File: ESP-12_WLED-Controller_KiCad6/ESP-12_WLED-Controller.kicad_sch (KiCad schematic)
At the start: 24 parts, among them J1 Conn_01x04_Male, J2 Conn_01x04_Male, Q1 IRLML6344, Q2 IRF7410, SW1 SW_RST, U1 TS1117-3.3, U2 ESP-12E, U4 74LVC1G125

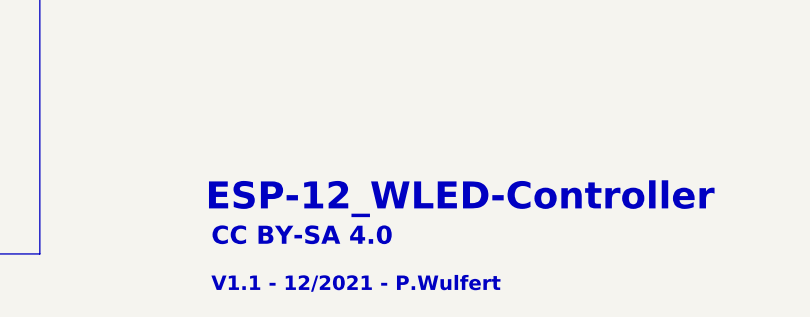
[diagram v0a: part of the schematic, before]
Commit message: V1.2
change Gate Resistor to 300 Ohm
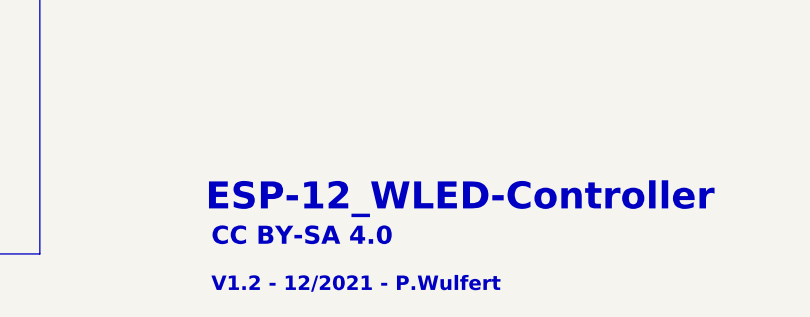
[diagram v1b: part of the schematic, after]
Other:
- note added: "V1.2 - 12/2021 - P.Wulfert"
- note removed: "V1.1 - 12/2021 - P.Wulfert"
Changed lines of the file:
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@@
     (effects (font (size 0.889 0.889)) (justify left bottom))
   )
-  (text "V1.1 - 12/2021 - P.Wulfert" (at 178.435 180.34 0)
+  (text "V1.2 - 12/2021 - P.Wulfert" (at 178.435 180.34 0)
     (effects (font (size 1.6002 1.6002) (thickness 0.32) bold) (justify left bottom))
   )

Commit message: Update to V2.0
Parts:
- removed J2: Conn_01x04_Male, Connector_PinHeader_2.54mm:PinHeader_1x04_P2.54mm_Vertical, symbol Connector:Conn_01x04_Male
- added J2: Conn_01x05_Male, Connector_PinHeader_2.54mm:PinHeader_1x05_P2.54mm_Vertical, symbol Connector:Conn_01x05_Male
- added JP2: Jumper_2_Open, Jumper:SolderJumper-2_P1.3mm_Open_TrianglePad1.0x1.5mm, symbol Jumper:Jumper_2_Open
- added aC2: 100µF, Capacitor_SMD:C_0805_2012Metric_Pad1.18x1.45mm_HandSolder, symbol Device:C
- C1, C2: LCSC (none) -> C1713
- C3: LCSC (none) -> C49678
- C4: LCSC (none) -> C189254
- D1: LCSC (none) -> C2480
- JP1: LCSC (none) -> C390678
- Q1: LCSC (none) -> C693370
- Q2: LCSC (none) -> C152423
- R1, R2, R3, R4, R5, R7, R8, R9: LCSC (none) -> C17617
- R6: LCSC (none) -> C114564
- SW1: LCSC (none) -> C329185
- U1: LCSC (none) -> C410833
- U2: LCSC (none) -> C82891
- U4: LCSC (none) -> C12518
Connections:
- net +3V3: now also J2.4 (Pin_4), aC2.1
- net GND: now also J2.1 (Pin_1), aC2.2
- net GPIO4_5: now also JP2.1 (A)
- net RX: now also J2.3 (Pin_3)
- net TX: now also J2.2 (Pin_2)
- net A0: now reaches U2.2 (ADC)
- net A0: now also J2.5 (Pin_5)
- net DATA: now reaches J1.3 (Pin_3), R6.1
- net DATA: now also JP2.2 (B)
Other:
- note added: "Additional Capacitor Value depends on taken LDO."
- note added: "Bypass jumper for R6, if any problems with data signal."
- note added: "Expose A0 Analog input can be used for sound reactive features."
- note added: "Resistor value is not fixed! In some cases it's better to decrease the value. In very rare conditions, the strip will just run without a resistor."
- note added: "THT P-MOSFET Alternative to the SOIC type."
- note added: "V2.0 - 01/2022 - P.Wulfert"
- note removed: "V1.2 - 12/2021 - P.Wulfert"
- note removed: "use here an alternative THT P-MOSFET"
- moved on the sheet: C3, R7, R9, SW1, altQ2

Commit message: Update to V1.3
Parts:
- removed J1: Conn_01x04_Male, TerminalBlock_Phoenix:TerminalBlock_Phoenix_MKDS-1,5-4-5.08_1x04_P5.08mm_Horizontal, symbol Connector:Conn_01x04_Male
- removed J2: Conn_01x05_Male, Connector_PinHeader_2.54mm:PinHeader_1x05_P2.54mm_Vertical, symbol Connector:Conn_01x05_Male
- removed altQ2: alt. MOSFET, Package_TO_SOT_THT:TO-220-3_Vertical, symbol Transistor_FET:IRF9540N
- added C5: 100nF, Capacitor_SMD:C_0805_2012Metric_Pad1.18x1.45mm_HandSolder, symbol Device:C
- added J1: Screw_Terminal_01x05, TerminalBlock:TerminalBlock_bornier-5_P5.08mm, symbol Connector:Screw_Terminal_01x05
- added J2: Conn_01x04_Male, Connector_PinSocket_2.54mm:PinSocket_1x04_P2.54mm_Vertical, symbol Connector:Conn_01x04_Male
- C1, C3: footprint Capacitor_SMD:C_0805_2012Metric_Pad1.15x1.40mm_HandSolder -> Capacitor_SMD:C_0805_2012Metric_Pad1.18x1.45mm_HandSolder
- C2: value 10µF -> 47F; footprint Capacitor_SMD:C_0805_2012Metric_Pad1.15x1.40mm_HandSolder -> Capacitor_SMD:C_0805_2012Metric_Pad1.18x1.45mm_HandSolder
- JP1: value Jumper -> BTN/FLASH
- JP2: footprint Jumper:SolderJumper-2_P1.3mm_Open_TrianglePad1.0x1.5mm -> Jumper:SolderJumper-2_P1.3mm_Open_RoundedPad1.0x1.5mm
- R1, R2, R3, R4, R5, R6, R7, R8, R9: footprint Resistor_SMD:R_0805_2012Metric_Pad1.15x1.40mm_HandSolder -> Resistor_SMD:R_0805_2012Metric_Pad1.20x1.40mm_HandSolder
- SW1: LCSC C329185 -> (none)
- U4: footprint Package_SO:TSOP-5_1.65x3.05mm_P0.95mm -> Package_TO_SOT_SMD:SOT-23-5
- aC2: footprint Capacitor_SMD:C_0805_2012Metric_Pad1.18x1.45mm_HandSolder -> Capacitor_SMD:C_1206_3216Metric_Pad1.33x1.80mm_HandSolder
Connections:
- net +3V3: now also J2.4 (Pin_4)
- net +5V: now also C5.2, J1.2 (Pin_2)
- net DATA: now also J1.4 (Pin_4)
- net GND: now also C5.1, J1.1 (Pin_1), J1.5 (Pin_5), J2.1 (Pin_1); no longer U4.1
- net RX: now also J2.3 (Pin_3)
- net TX: now also J2.2 (Pin_2)
- net WS-Strip_VCC: now also J1.3 (Pin_3)
- net OE: now reaches Q1.3 (D), Q2.4 (G), R7.2
- net OE: now also U4.1
- net GPIO2 renamed DATA_3.3
- net DATA_3.3: now also U4.2
- net GPIO4_3.3: no longer names the net of U2.19 (GPIO4)
- net GPIO4_3.3: no longer U4.2
- net GPIO4_5 renamed DATA_5
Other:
- note added: "V1.3 - 01/2022 - P.Wulfert"
- note removed: "Expose A0 Analog input can be used for sound reactive features."
- note removed: "Resistor value is not fixed! In some cases it's better to decrease the value. In very rare conditions, the strip will just run without a resistor."
- note removed: "THT P-MOSFET Alternative to the SOIC type."
- note removed: "V2.0 - 01/2022 - P.Wulfert"
- moved on the sheet: C3, C4, D1, JP1, JP2, Q1, Q2, R6, R7, R8, R9, U4
